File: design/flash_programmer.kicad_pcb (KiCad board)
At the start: 2 copper layers, 82.5 x 52.1 mm, 44 parts, among them P1 ISP, P2 USB_B, P3 CONN_01X02, P4 CONN_01X03, P5 CONN_01X03, U1 MAX662A, U2 2N3906, U3 ATMEGA328P_TQFN, U4 GLS27SF010, U5 74HC595, U6 74HC595, U7 FT230X

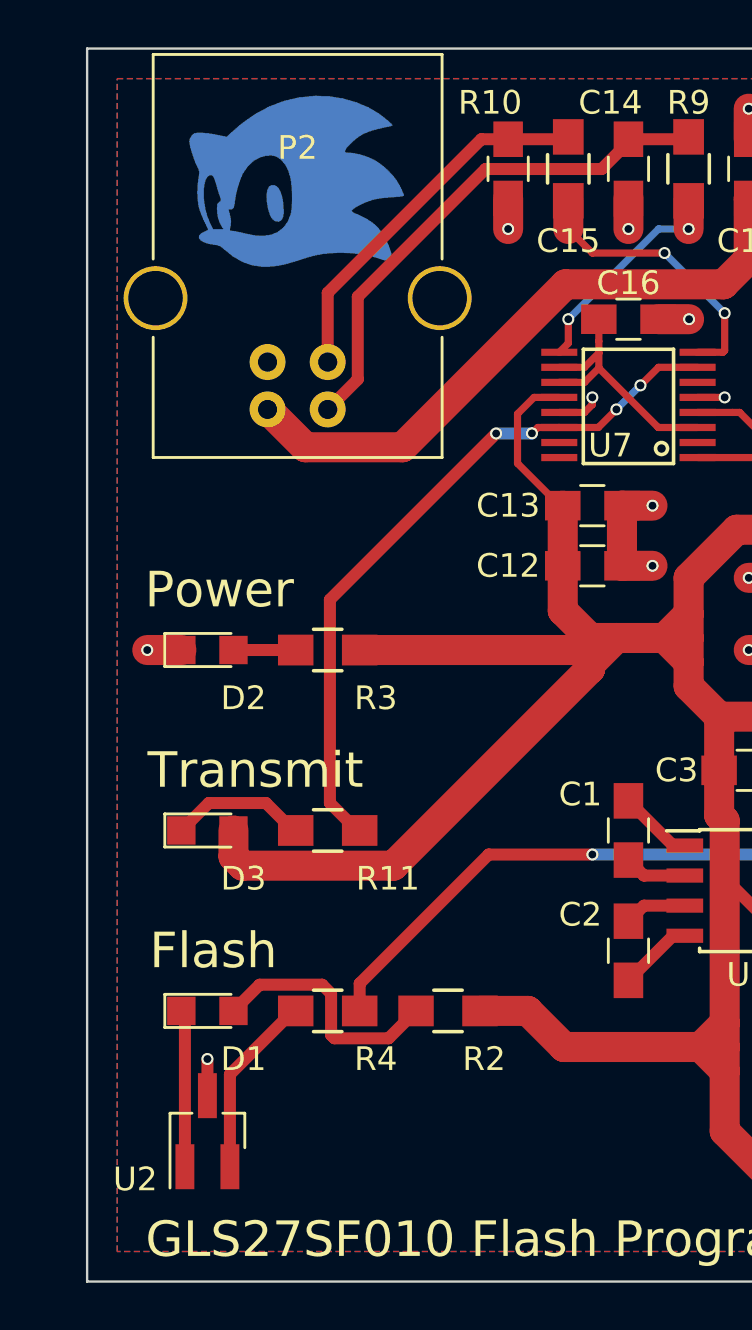
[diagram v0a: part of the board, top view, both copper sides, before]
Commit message: Fix errors in PCB design
Fixed the pin order on the 2n3906 transistor for the flash indicator LED.

Corrected positions of labels for C15 and R10.
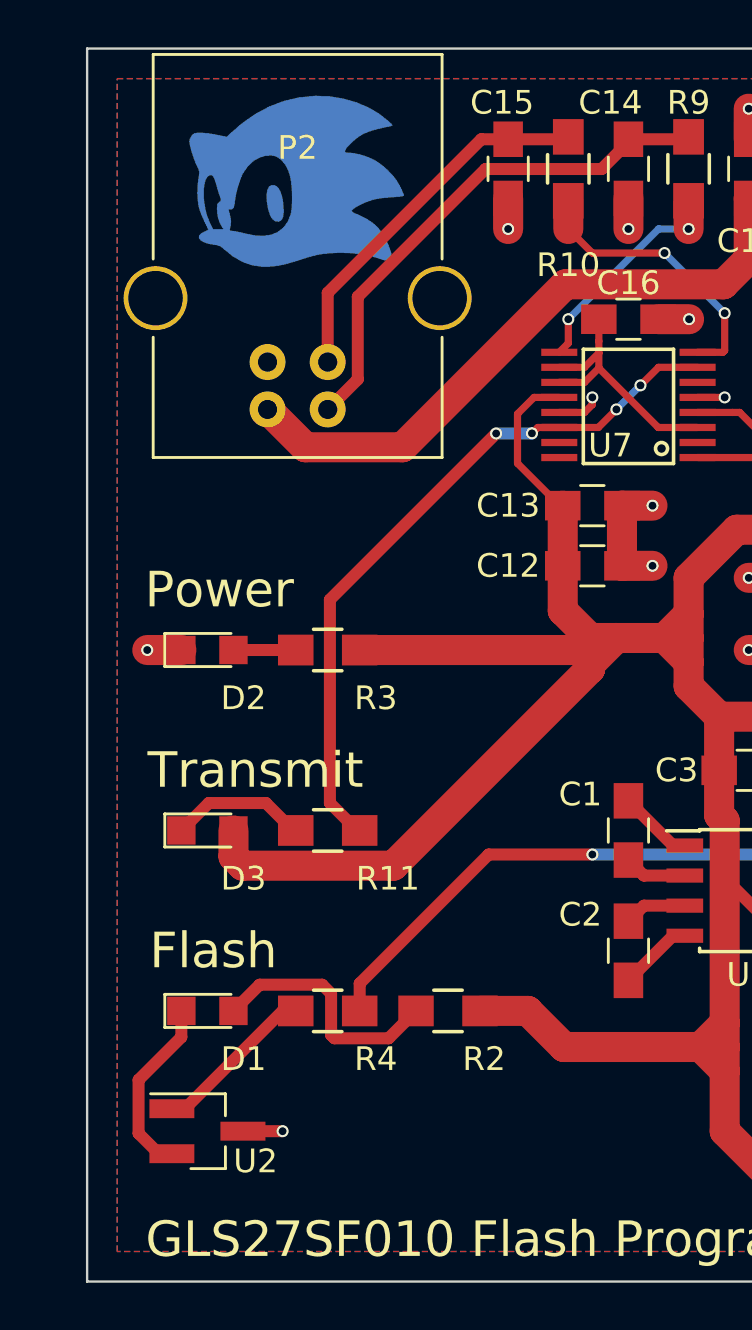
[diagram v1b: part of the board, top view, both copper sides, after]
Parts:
- turned U2 to 0 degrees
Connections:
- U2 pad 1: Net-(D1-Pad1) -> Net-(R4-Pad2)
- U2 pad 2: Net-(R4-Pad2) -> Net-(D1-Pad1)
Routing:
- net Net-(D1-Pad1): track 6.64 -> 7.90 mm
- net Net-(R4-Pad2): track 7.79 -> 7.04 mm
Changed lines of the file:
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@@
     (thickness 1.6)
     (drawings 32)
-    (tracks 654)
+    (tracks 659)
     (zones 0)
     (modules 44)
@@
     (tags "capacitor 0805")
     (attr smd)
-    (fp_text reference C15 (at 3.048 -2.54 540) (layer F.SilkS)
+    (fp_text reference C15 (at -2.794 0.254 540) (layer F.SilkS)
       (effects (font (size 1 1) (thickness 0.15)))
     )
@@
     (tags "resistor 0805")
     (attr smd)
-    (fp_text reference R10 (at 2.794 -3.302 360) (layer F.SilkS)
+    (fp_text reference R10 (at -4.064 0 360) (layer F.SilkS)
       (effects (font (size 1 1) (thickness 0.15)))
     )
@@
   )
   (module TO_SOT_Packages_SMD:SOT-23_Handsoldering (layer F.Cu)
-    (at 40.64 81.28 90)
+    (at 40.64 81.28)
     (descr "SOT-23, Handsoldering")
     (tags SOT-23)
     (attr smd)
-    (fp_text reference U2 (at -2.032 -3.048 180) (layer F.SilkS)
-      (effects (font (size 1 1) (thickness 0.15)))
-    )
-    (fp_text value 2N3906 (at 0 2.5 90) (layer F.Fab)
+    (fp_text reference U2 (at 2.032 1.27 180) (layer F.SilkS)
+      (effects (font (size 1 1) (thickness 0.15)))
+    )
+    (fp_text value 2N3906 (at 0 2.5) (layer F.Fab)
       (effects (font (size 1 1) (thickness 0.15)))
     )
@@
     (fp_line (start -0.7 -1.02) (end -0.7 1.52) (layer F.Fab) (width 0.1))
     (fp_line (start 0.76 1.58) (end -0.7 1.58) (layer F.SilkS) (width 0.12))
-    (pad 1 smd rect (at -1.5 -0.95 90) (size 1.9 0.8) (layers F.Cu F.Paste F.Mask)
+    (pad 1 smd rect (at -1.5 -0.95) (size 1.9 0.8) (layers F.Cu F.Paste F.Mask)
+      (net 28 "Net-(R4-Pad2)"))
+    (pad 2 smd rect (at -1.5 0.95) (size 1.9 0.8) (layers F.Cu F.Paste F.Mask)
       (net 13 "Net-(D1-Pad1)"))
-    (pad 2 smd rect (at -1.5 0.95 90) (size 1.9 0.8) (layers F.Cu F.Paste F.Mask)
-      (net 28 "Net-(R4-Pad2)"))
-    (pad 3 smd rect (at 1.5 0 90) (size 1.9 0.8) (layers F.Cu F.Paste F.Mask)
+    (pad 3 smd rect (at 1.5 0) (size 1.9 0.8) (layers F.Cu F.Paste F.Mask)
       (net 5 GND))
     (model TO_SOT_Packages_SMD.3dshapes/SOT-23.wrl
@@
   (segment (start 60.8 71.755) (end 59.075 71.755) (width 0.508) (layer F.Cu) (net 4))
   (segment (start 59.075 71.755) (end 58.42 72.41) (width 0.508) (layer F.Cu) (net 4))
+  (segment (start 42.14 81.28) (end 43.815 81.28) (width 0.508) (layer F.Cu) (net 5))
+  (via (at 43.815 81.28) (size 0.508) (drill 0.3302) (layers F.Cu B.Cu) (net 5))
   (segment (start 116.332 47.244) (end 116.332 52.324) (width 0.4064) (layer F.Cu) (net 5))
   (via (at 116.332 52.324) (size 0.508) (drill 0.3302) (layers F.Cu B.Cu) (net 5))
@@
   (segment (start 39.54 60.96) (end 38.1 60.96) (width 1.27) (layer F.Cu) (net 5))
   (via (at 38.1 60.96) (size 0.508) (drill 0.3302) (layers F.Cu B.Cu) (net 5))
-  (segment (start 40.64 79.78) (end 40.64 78.232) (width 0.508) (layer F.Cu) (net 5))
-  (via (at 40.64 78.232) (size 0.508) (drill 0.3302) (layers F.Cu B.Cu) (net 5))
   (segment (start 113.284 74.95) (end 113.284 73.66) (width 1.27) (layer F.Cu) (net 5))
   (via (at 113.284 73.66) (size 0.508) (drill 0.3302) (layers F.Cu B.Cu) (net 5))
@@
   (segment (start 45.862799 77.215761) (end 46.005038 77.358) (width 0.508) (layer F.Cu) (net 12))
   (segment (start 46.005038 77.358) (end 48.292 77.358) (width 0.508) (layer F.Cu) (net 12))
-  (segment (start 39.69 82.78) (end 39.69 76.35) (width 0.508) (layer F.Cu) (net 13))
+  (segment (start 39.14 82.23) (end 38.59 82.23) (width 0.508) (layer F.Cu) (net 13))
+  (segment (start 38.59 82.23) (end 37.732799 81.372799) (width 0.508) (layer F.Cu) (net 13))
+  (segment (start 37.732799 81.372799) (end 37.732799 79.115201) (width 0.508) (layer F.Cu) (net 13))
+  (segment (start 37.732799 79.115201) (end 39.54 77.308) (width 0.508) (layer F.Cu) (net 13))
+  (segment (start 39.54 77.308) (end 39.54 76.2) (width 0.508) (layer F.Cu) (net 13))
   (segment (start 39.69 76.35) (end 39.54 76.2) (width 0.508) (layer F.Cu) (net 13))
   (segment (start 41.74 60.96) (end 44.37 60.96) (width 0.508) (layer F.Cu) (net 14))
@@
   (segment (start 72.892 61.22) (end 73.152 60.96) (width 0.4064) (layer F.Cu) (net 27))
   (segment (start 71.4 61.22) (end 72.892 61.22) (width 0.4064) (layer F.Cu) (net 27))
-  (segment (start 41.59 82.78) (end 41.59 78.88) (width 0.508) (layer F.Cu) (net 28))
-  (segment (start 41.59 78.88) (end 44.27 76.2) (width 0.508) (layer F.Cu) (net 28))
+  (segment (start 39.14 80.33) (end 39.69 80.33) (width 0.508) (layer F.Cu) (net 28))
+  (segment (start 39.69 80.33) (end 43.82 76.2) (width 0.508) (layer F.Cu) (net 28))
+  (segment (start 43.82 76.2) (end 44.37 76.2) (width 0.508) (layer F.Cu) (net 28))
   (segment (start 44.27 76.2) (end 44.37 76.2) (width 0.508) (layer F.Cu) (net 28))
   (segment (start 81 57.22) (end 84.8664 57.22) (width 0.4064) (layer F.Cu) (net 29))

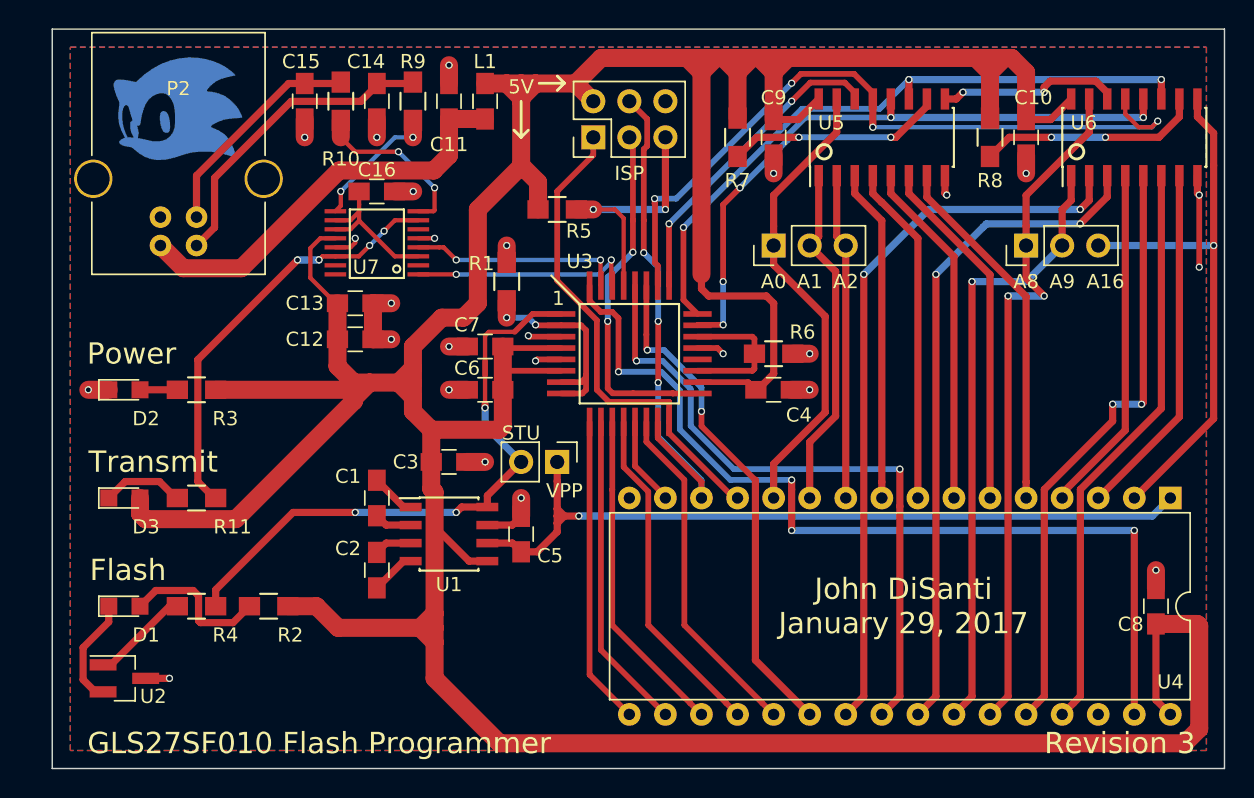
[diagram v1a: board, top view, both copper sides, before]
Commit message: Redo PCB: fix errors and shrink
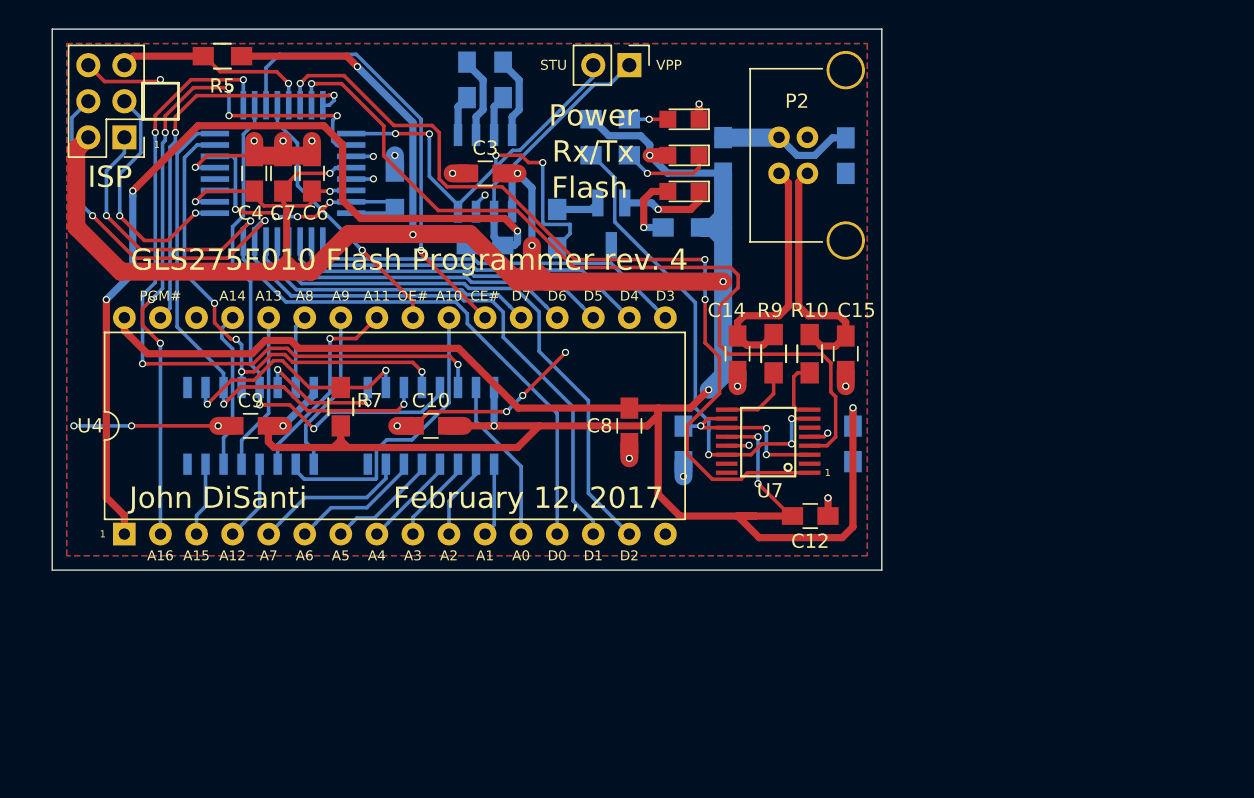
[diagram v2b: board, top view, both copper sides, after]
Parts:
- removed G***: LOGO, logo:logo
- removed P4, P5: CONN_01X03, Pin_Headers:Pin_Header_Straight_1x03_Pitch2.54mm
- removed R6, R8: 10k, Resistors_SMD:R_0805_HandSoldering
- C1, C11, C13, C16, C2, C5, L1, R1, R11, R2, R3, R4, U1, U2, U3, U5, U6: moved to B.Cu
- P2: footprint Connect:USB_B -> USB_B_Female:USB_B
- moved U4 73.7 mm to (40.6, 71.1), turned to 90 degrees
- moved U6 65.5 mm to (49.5, 63.5)
- moved D1 49.0 mm to (80.0, 47.0), turned to 180 degrees
- moved U2 46.9 mm to (74.9, 49.3), turned to 270 degrees
- moved C10 46.6 mm to (62.2, 63.5), turned to 0 degrees
- moved D3 46.2 mm to (80.0, 44.5), turned to 180 degrees
- moved P2 44.2 mm to (86.7, 43.2), turned to 0 degrees
- moved D2 43.7 mm to (80.0, 41.9), turned to 180 degrees
- moved C9 42.1 mm to (49.5, 63.5), turned to 0 degrees
- moved C15 42.0 mm to (91.4, 58.4)
- moved C4 39.6 mm to (49.8, 45.7), turned to 270 degrees
- moved R2 39.5 mm to (79.9, 49.5)
- moved C8 39.2 mm to (76.2, 63.5), turned to 90 degrees
- moved R11 37.8 mm to (74.8, 44.5), turned to 180 degrees
- moved U5 37.7 mm to (62.2, 63.5)
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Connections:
- R1 pad 1: Net-(R1-Pad1) -> /UNUSED_GND
- U3 pad 19: Net-(R6-Pad2) -> /UNUSED_GND
- U3 pad 2: Net-(R1-Pad1) -> /A16
- U3 pad 22: Net-(R6-Pad2) -> /UNUSED_GND
- U3 pad 7: Net-(R1-Pad1) -> /UNUSED_GND
- U3 pad 8: Net-(R1-Pad1) -> /UNUSED_GND
- U6 pad 10: Net-(R8-Pad1) -> Net-(R7-Pad1)
- U6 pad 9: /A16 -> Net-(U6-Pad9)
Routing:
- net /RXD: track 15.9 -> 62.2 mm, vias 2 -> 3
- net /TXD: track 15.0 -> 59.7 mm, vias 2 -> 1
- net /A8: track 48.8 -> 5.18 mm, vias 2 -> 0
- net /PGM#: track 65.0 -> 27.7 mm, vias 4 -> 2
- net VCC: track 331.6 -> 296.3 mm, vias 0 -> 15
- net /D2: track 6.25 -> 39.5 mm
- net /A11: track 47.3 -> 14.3 mm, vias 2 -> 1
- net /A9: track 43.6 -> 11.6 mm, vias 1 -> 0
- net /A13: track 42.5 -> 11.1 mm, vias 2 -> 0
- net /A10: track 51.3 -> 20.9 mm, vias 2 -> 0
- net /A14: track 40.8 -> 11.2 mm
- net /SER: track 22.3 -> 51.7 mm, vias 2 -> 4
- net /OE#: track 46.4 -> 18.9 mm, vias 2 -> 1
- net /D1: track 36.9 -> 64.0 mm, vias 3 -> 2
- net /VPP: track 55.8 -> 79.3 mm, vias 1 -> 3
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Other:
- board size 82.5 x 52.1 mm -> 58.4 x 38.1 mm
- net class Default: clearance 0.2032 -> 0.1778; trace_width 0.3048 -> 0.254
- rule trace_clearance: 0.2032 -> 0.1778
- rule trace_min: 0.1524 -> 0.2032
- board text added: "1"
- board text added: "A10"
- board text added: "A11"
- board text added: "A12"
- board text added: "A13"
- board text added: "A14"
- board text added: "A15"
- board text added: "A3"
- board text added: "A4"
- board text added: "A5"
- board text added: "A6"
- board text added: "A7"
- board text added: "CE#"
- board text added: "D0"
- board text added: "D1"
- board text added: "D2"
- board text added: "D3"
- board text added: "D4"
- board text added: "D5"
- board text added: "D6"
- board text added: "D7"
- board text added: "February 12, 2017"
- board text added: "GLS275F010 Flash Programmer rev. 4"
- board text added: "John DiSanti"
- board text added: "OE#"
- board text added: "PGM#"
- board text added: "Rx/Tx"
- board text removed: "5V"
- board text removed: "GLS27SF010 Flash Programmer"
- board text removed: "John DiSanti January 29, 2017"
- board text removed: "Revision 3"
- board text removed: "Transmit"

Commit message: Revise the PCB
Added a ground test point, and enlarged annular rings around vias.
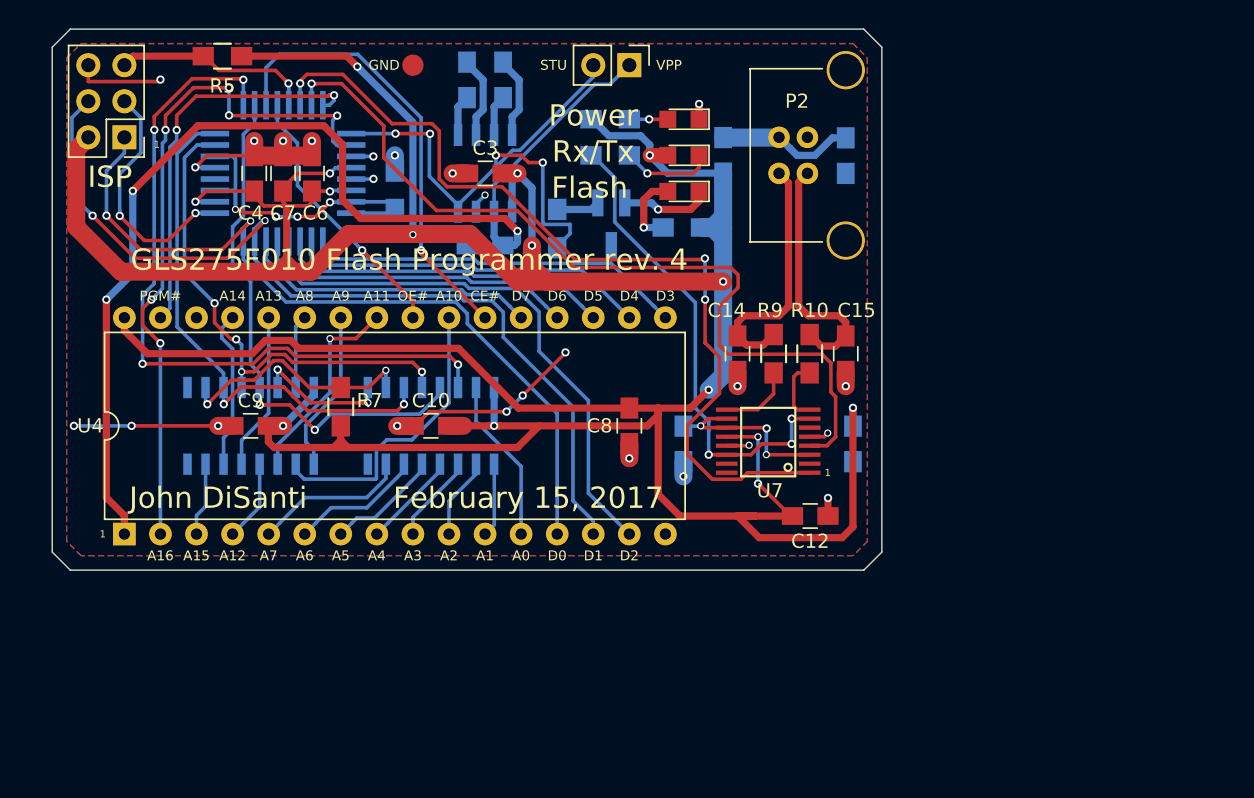
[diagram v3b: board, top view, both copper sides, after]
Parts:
- added GND: Measurement_Point_Round-SMD-Pad_Small, Measurement_Points:Measurement_Point_Round-SMD-Pad_Small, F.Cu at (61.0, 38.1)
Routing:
- net GND: track 60.1 -> 60.7 mm
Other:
- outline, holes or cut-outs redrawn
- net class Default: via_dia 0.508 -> 0.5842
- board text added: "February 15, 2017"
- board text removed: "February 12, 2017"

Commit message: Revise the silkscreens on the PCB
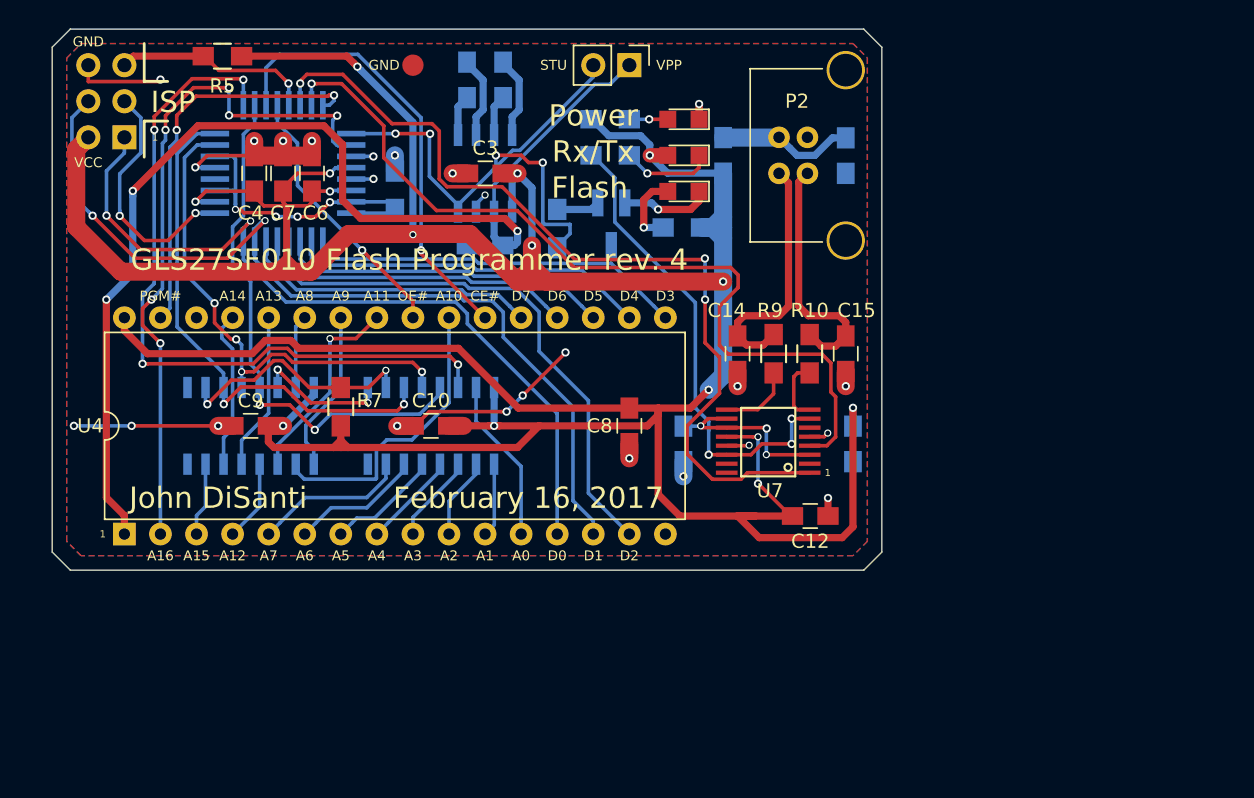
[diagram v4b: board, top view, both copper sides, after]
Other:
- board text added: "February 16, 2017"
- board text added: "GLS27SF010 Flash Programmer rev. 4"
- board text added: "GND"
- board text added: "VCC"
- board text removed: "February 15, 2017"
- board text removed: "GLS275F010 Flash Programmer rev. 4"
